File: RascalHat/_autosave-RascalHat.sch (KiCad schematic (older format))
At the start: 23 parts, among them P1 Conn_01x06, U1 Conn_01x04, X1 Conn_01x02, X2 Conn_01x02, X3 Conn_01x02

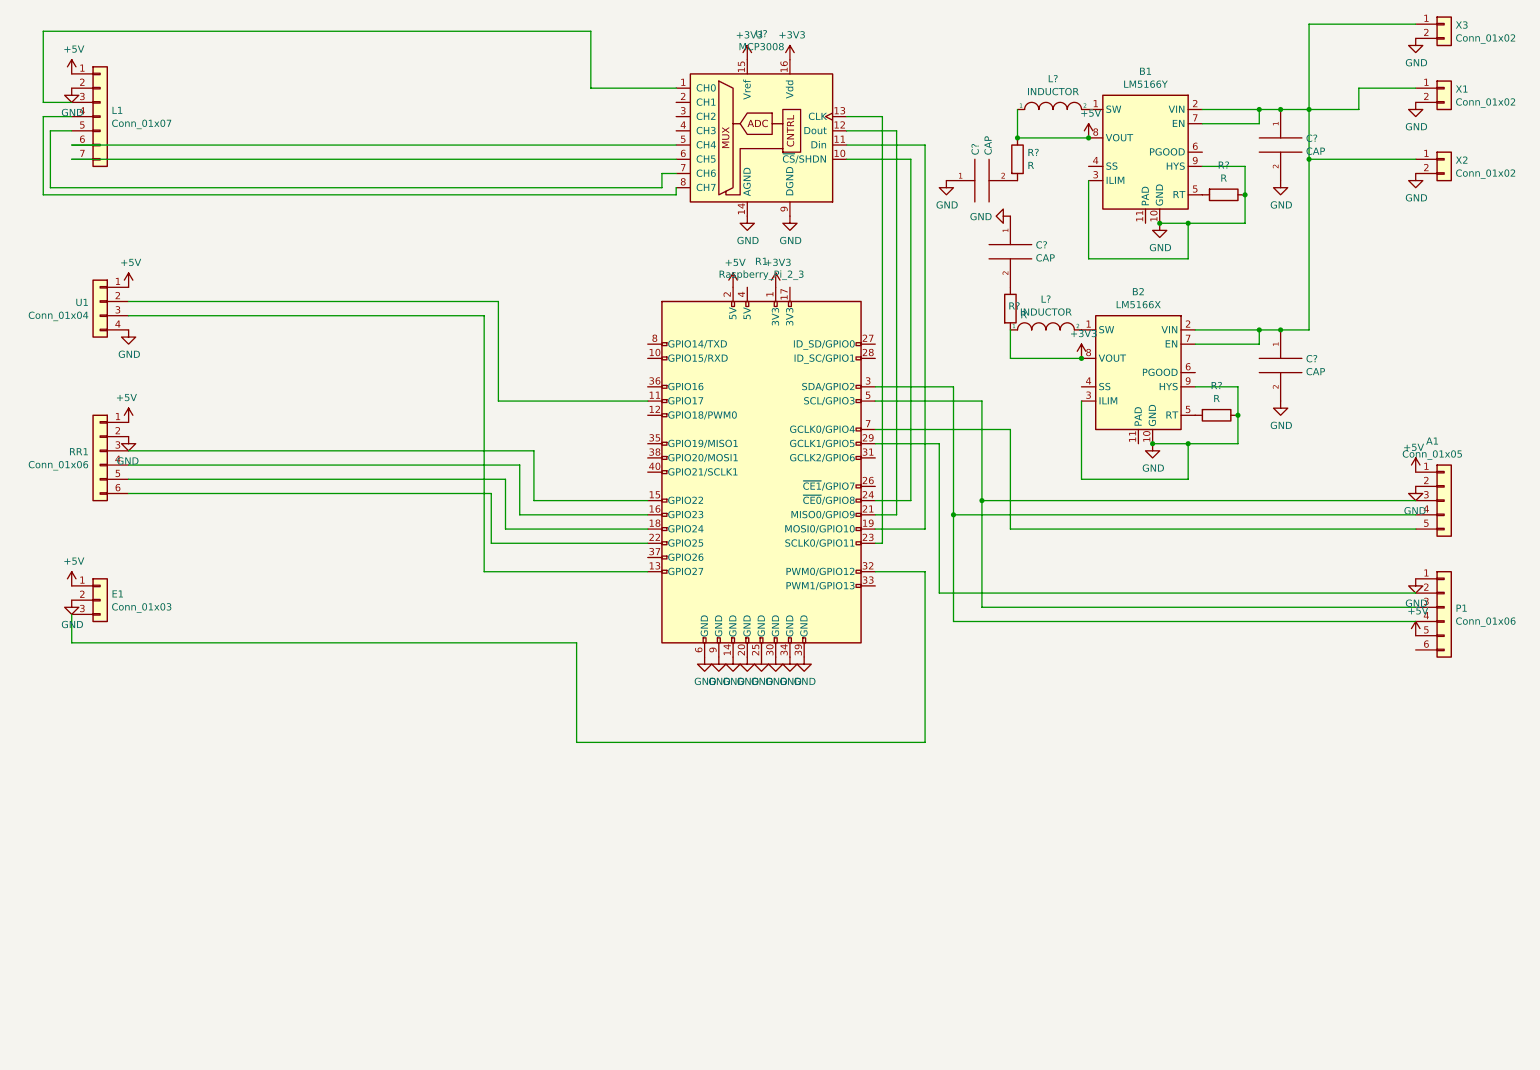
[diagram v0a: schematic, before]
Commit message: update schematic
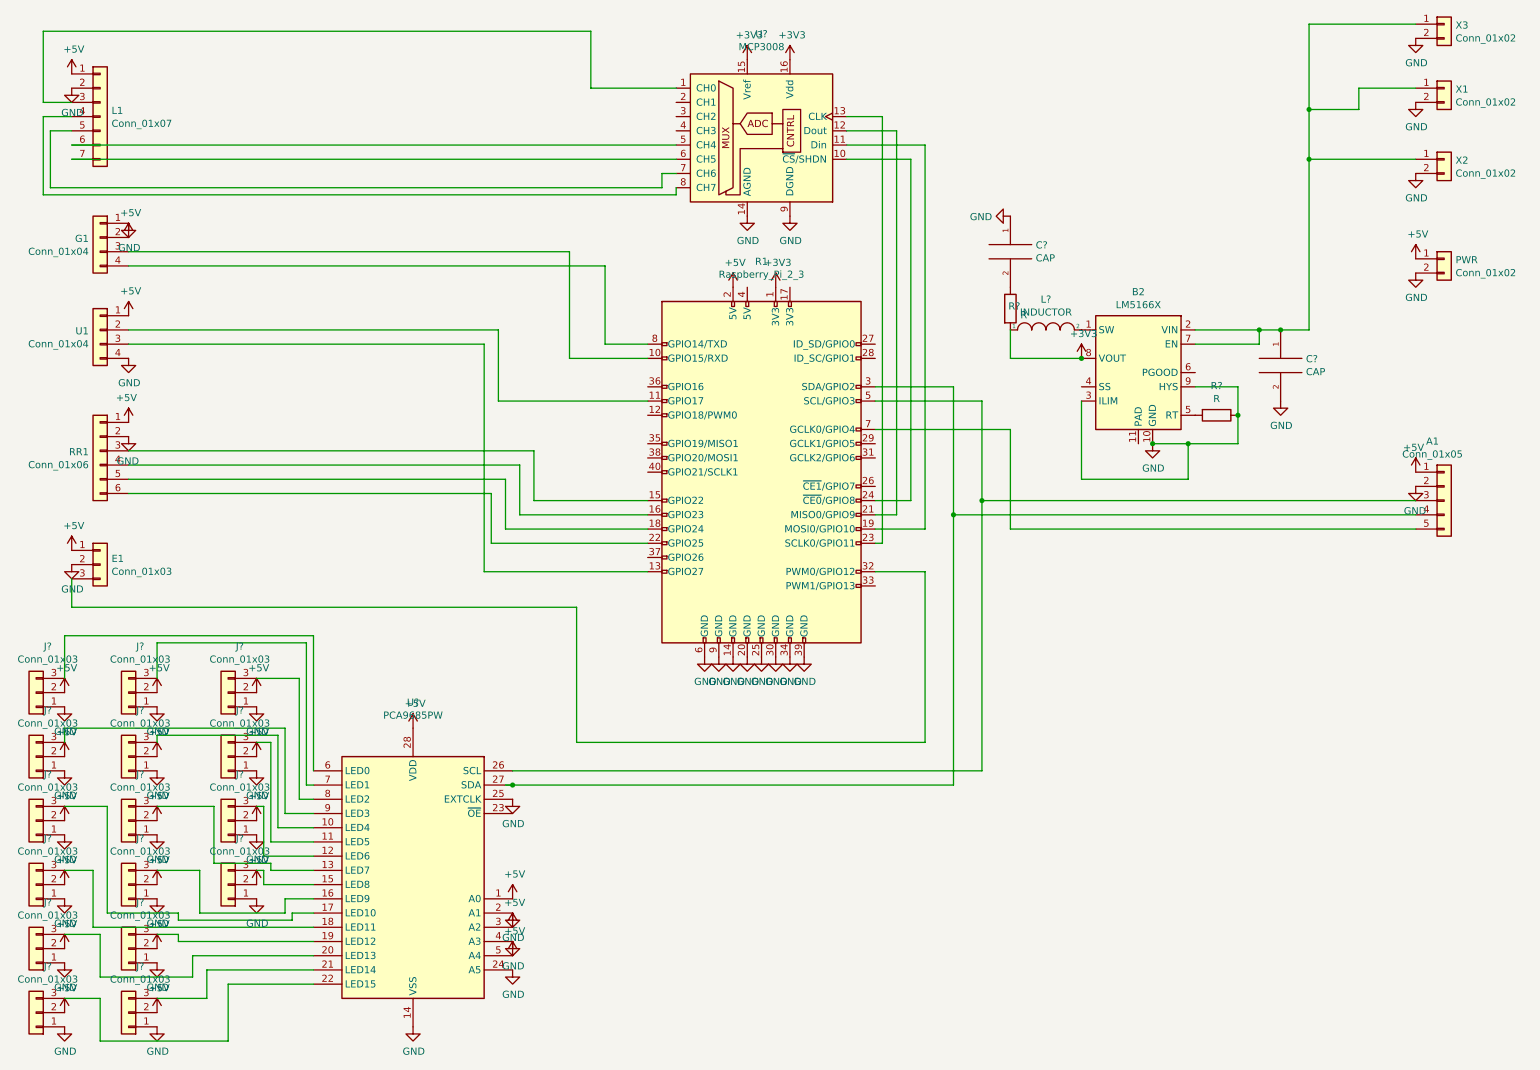
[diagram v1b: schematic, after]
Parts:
- removed B1: LM5166Y, Package_SON:Texas_S-PVSON-N10_ThermalVias, symbol Regulator_Switching:LM5166Y
- removed C? (x2): CAP, symbol pspice:CAP
- removed L?: INDUCTOR, symbol pspice:INDUCTOR
- removed P1: Conn_01x06, symbol Connector_Generic:Conn_01x06
- removed R? (x2): R, symbol Device:R
- added G1: Conn_01x04, symbol Connector_Generic:Conn_01x04
- added J? (x16): Conn_01x03, symbol Connector_Generic:Conn_01x03
- added PWR: Conn_01x02, symbol Connector_Generic:Conn_01x02
- added U?: PCA9685PW, Package_SO:TSSOP-28_4.4x9.7mm_P0.65mm, symbol Driver_LED:PCA9685PW
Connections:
- net +5V: now also G1.2 (Pin_2), J?.2 (Pin_2), J?.2 (Pin_2), J?.2 (Pin_2), J?.2 (Pin_2), J?.2 (Pin_2), J?.2 (Pin_2), J?.2 (Pin_2), J?.2 (Pin_2), J?.2 (Pin_2), J?.2 (Pin_2), J?.2 (Pin_2), J?.2 (Pin_2), J?.2 (Pin_2), J?.2 (Pin_2), J?.2 (Pin_2), J?.2 (Pin_2), PWR.1 (Pin_1), U?.1 (A0), U?.28 (VDD), U?.3 (A2), U?.5 (A4)
- net GND: now also G1.1 (Pin_1), J?.1 (Pin_1), J?.1 (Pin_1), J?.1 (Pin_1), J?.1 (Pin_1), J?.1 (Pin_1), J?.1 (Pin_1), J?.1 (Pin_1), J?.1 (Pin_1), J?.1 (Pin_1), J?.1 (Pin_1), J?.1 (Pin_1), J?.1 (Pin_1), J?.1 (Pin_1), J?.1 (Pin_1), J?.1 (Pin_1), J?.1 (Pin_1), PWR.2 (Pin_2), U?.14 (VSS), U?.2 (A1), U?.24 (A5), U?.25 (EXTCLK), U?.4 (A3)
- net at R1.10 (GPIO15/RXD): now also G1.3 (Pin_3)
- net at A1.4 (Pin_4), R1.3 (SDA/GPIO2): now also U?.27 (SDA)
- net at A1.3 (Pin_3), R1.5 (SCL/GPIO3): now also U?.26 (SCL)
- net at R1.8 (GPIO14/TXD): now also G1.4 (Pin_4)
- new net: J?.3 (Pin_3), U?.10 (LED4)
- new net: J?.3 (Pin_3), U?.11 (LED5)
- new net: J?.3 (Pin_3), U?.12 (LED6)
- new net: J?.3 (Pin_3), U?.13 (LED7)
- new net: J?.3 (Pin_3), U?.15 (LED8)
- new net: J?.3 (Pin_3), U?.16 (LED9)
- new net: J?.3 (Pin_3), U?.17 (LED10)
- new net: J?.3 (Pin_3), U?.18 (LED11)
- new net: J?.3 (Pin_3), U?.19 (LED12)
- new net: J?.3 (Pin_3), U?.20 (LED13)
- new net: J?.3 (Pin_3), U?.21 (LED14)
- new net: J?.3 (Pin_3), U?.22 (LED15)
- new net: J?.3 (Pin_3), U?.6 (LED0)
- new net: J?.3 (Pin_3), U?.7 (LED1)
- new net: J?.3 (Pin_3), U?.8 (LED2)
- new net: J?.3 (Pin_3), U?.9 (LED3)
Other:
- moved on the sheet: E1, U1
